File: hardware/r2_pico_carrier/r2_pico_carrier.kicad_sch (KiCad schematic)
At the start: 70 parts, among them J1 5V in, J2 OLED header, J3 Qwiic, J4 expansion, J5 USB-C 5V in, SW1 display, U1 PCA9517A

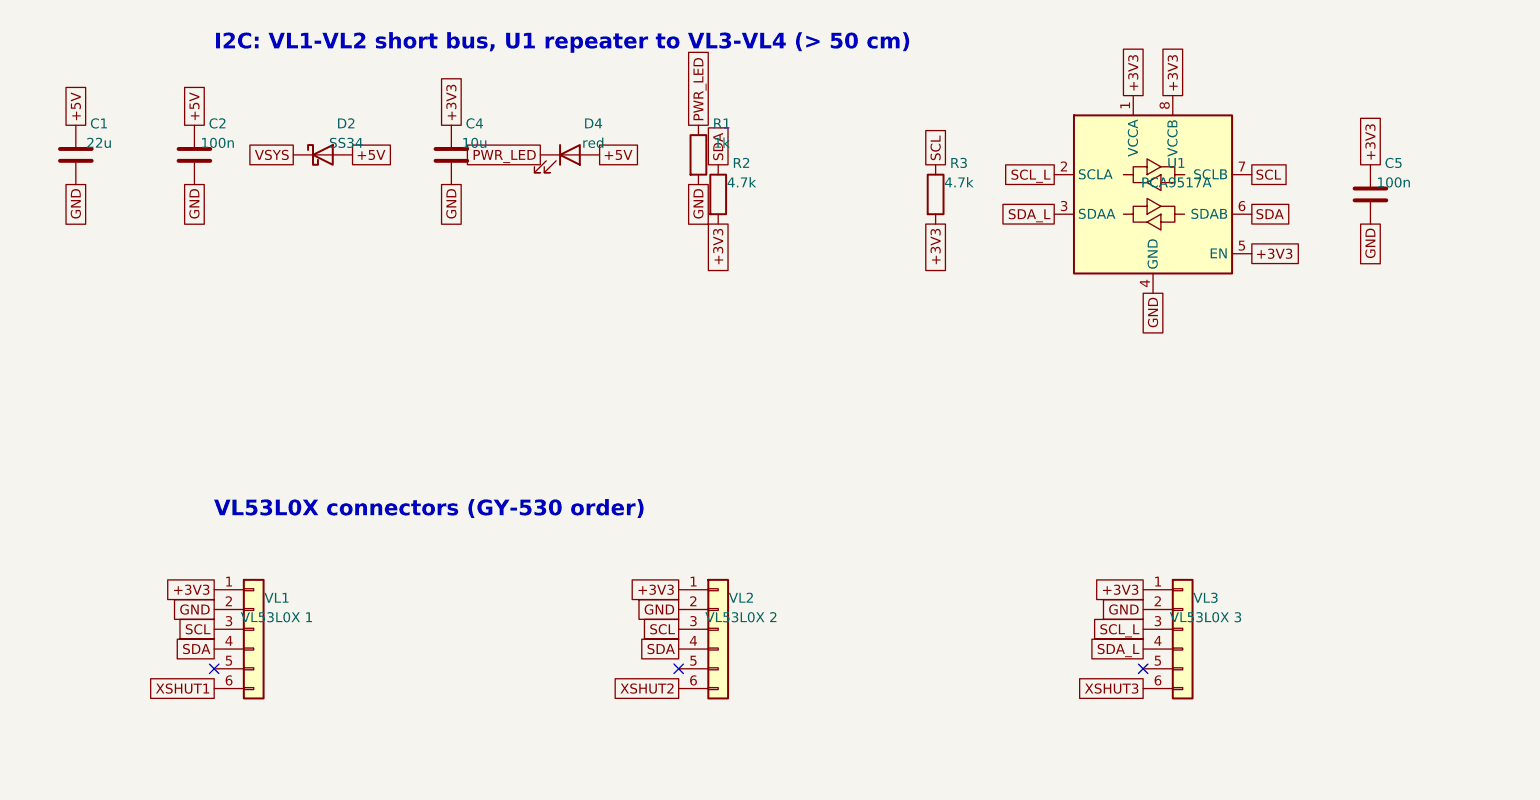
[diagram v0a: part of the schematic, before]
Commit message: Carrier board: all four VL53L0X behind the U1 repeater (any VL connector, cables up to 1 m; Pico bus keeps display, Qwiic, EXP); EXP header moved left, 3.4 mm clear of the OLED
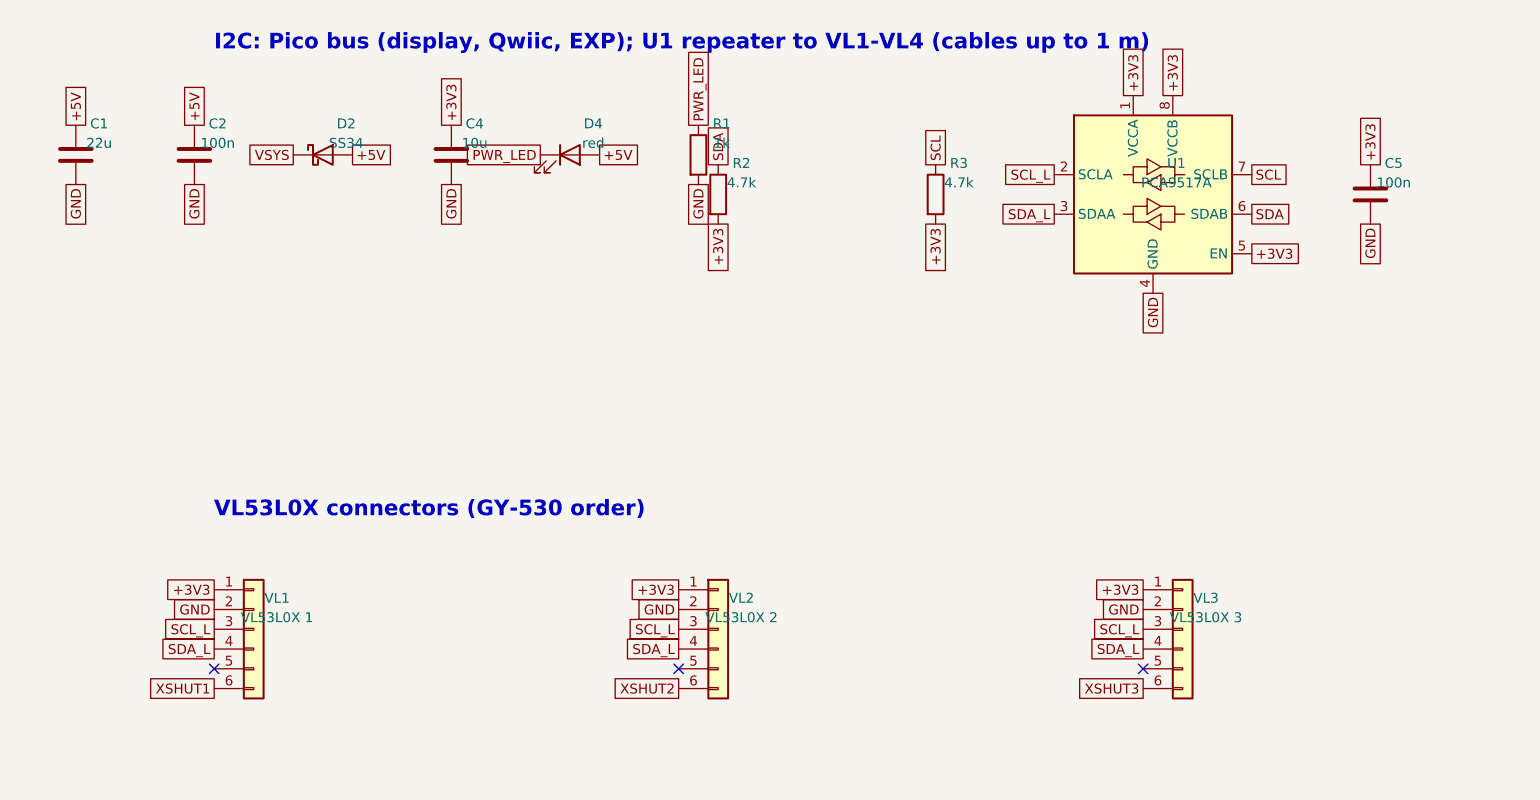
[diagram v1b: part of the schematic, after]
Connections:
- net SCL: no longer VL1.3 (Pin_3), VL2.3 (Pin_3)
- net SCL_L: now also VL1.3 (Pin_3), VL2.3 (Pin_3)
- net SDA: no longer VL1.4 (Pin_4), VL2.4 (Pin_4)
- net SDA_L: now also VL1.4 (Pin_4), VL2.4 (Pin_4)
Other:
- note added: "I2C: Pico bus (display, Qwiic, EXP); U1 repeater to VL1-VL4 (cables up to 1 m)"
- note removed: "I2C: VL1-VL2 short bus, U1 repeater to VL3-VL4 (> 50 cm)"
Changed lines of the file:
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@@
 (global_label "+3V3" (shape passive) (at 160.02 95.25 180) (fields_autoplaced yes) (effects (font (size 1.27 1.27)) (justify right)))
 (global_label "GND" (shape passive) (at 160.02 97.79 180) (fields_autoplaced yes) (effects (font (size 1.27 1.27)) (justify right)))
-(global_label "SCL" (shape passive) (at 160.02 100.33 180) (fields_autoplaced yes) (effects (font (size 1.27 1.27)) (justify right)))
-(global_label "SDA" (shape passive) (at 160.02 102.87 180) (fields_autoplaced yes) (effects (font (size 1.27 1.27)) (justify right)))
+(global_label "SCL_L" (shape passive) (at 160.02 100.33 180) (fields_autoplaced yes) (effects (font (size 1.27 1.27)) (justify right)))
+(global_label "SDA_L" (shape passive) (at 160.02 102.87 180) (fields_autoplaced yes) (effects (font (size 1.27 1.27)) (justify right)))
 (no_connect (at 160.02 105.41))
 (global_label "XSHUT1" (shape passive) (at 160.02 107.95 180) (fields_autoplaced yes) (effects (font (size 1.27 1.27)) (justify right)))
@@
 (global_label "+3V3" (shape passive) (at 219.71 95.25 180) (fields_autoplaced yes) (effects (font (size 1.27 1.27)) (justify right)))
 (global_label "GND" (shape passive) (at 219.71 97.79 180) (fields_autoplaced yes) (effects (font (size 1.27 1.27)) (justify right)))
-(global_label "SCL" (shape passive) (at 219.71 100.33 180) (fields_autoplaced yes) (effects (font (size 1.27 1.27)) (justify right)))
-(global_label "SDA" (shape passive) (at 219.71 102.87 180) (fields_autoplaced yes) (effects (font (size 1.27 1.27)) (justify right)))
+(global_label "SCL_L" (shape passive) (at 219.71 100.33 180) (fields_autoplaced yes) (effects (font (size 1.27 1.27)) (justify right)))
+(global_label "SDA_L" (shape passive) (at 219.71 102.87 180) (fields_autoplaced yes) (effects (font (size 1.27 1.27)) (justify right)))
 (no_connect (at 219.71 105.41))
 (global_label "XSHUT2" (shape passive) (at 219.71 107.95 180) (fields_autoplaced yes) (effects (font (size 1.27 1.27)) (justify right)))
@@
 (text "R2 Pico carrier — power" (exclude_from_sim no) (at 25 25 0) (effects (font (size 2 2) bold) (justify left)))
 (text "Pico 2 (plugs in, pins down)" (exclude_from_sim no) (at 25 95 0) (effects (font (size 2 2) bold) (justify left)))
-(text "I2C: VL1-VL2 short bus, U1 repeater to VL3-VL4 (> 50 cm)" (exclude_from_sim no) (at 160 25 0) (effects (font (size 2 2) bold) (justify left)))
+(text "I2C: Pico bus (display, Qwiic, EXP); U1 repeater to VL1-VL4 (cables up to 1 m)" (exclude_from_sim no) (at 160 25 0) (effects (font (size 2 2) bold) (justify left)))
 (text "VL53L0X connectors (GY-530 order)" (exclude_from_sim no) (at 160 85 0) (effects (font (size 2 2) bold) (justify left)))
 (text "HC-SR04 connectors, ECHO 1k/2k dividers" (exclude_from_sim no) (at 160 135 0) (effects (font (size 2 2) bold) (justify left)))
